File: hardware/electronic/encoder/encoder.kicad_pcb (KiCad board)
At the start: 2 copper layers, 26 x 29 mm, 10 parts, among them P1 CONN_01X04

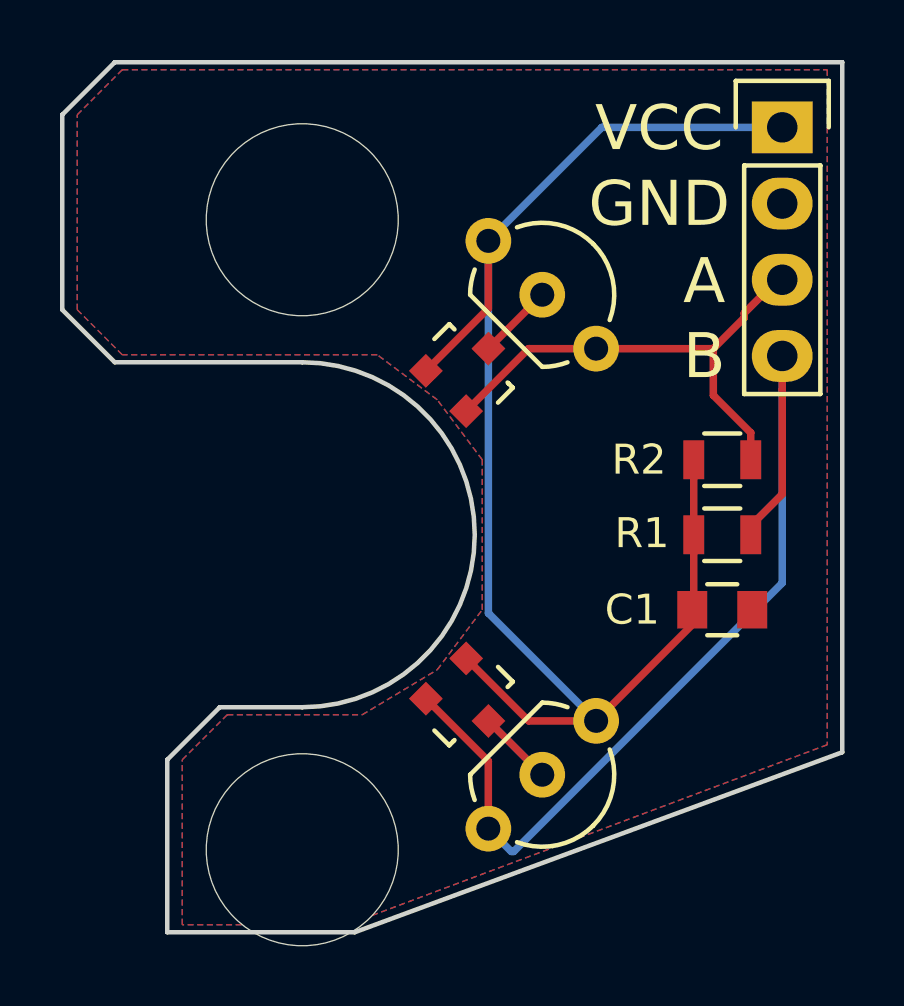
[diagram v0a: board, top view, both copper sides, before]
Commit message: HW: Start encoder rev-B
 - Remove smd footprints
 - Use bigger pads for passives
 - Fix missing connection
 - Improve hall effect footprint and silkscreen
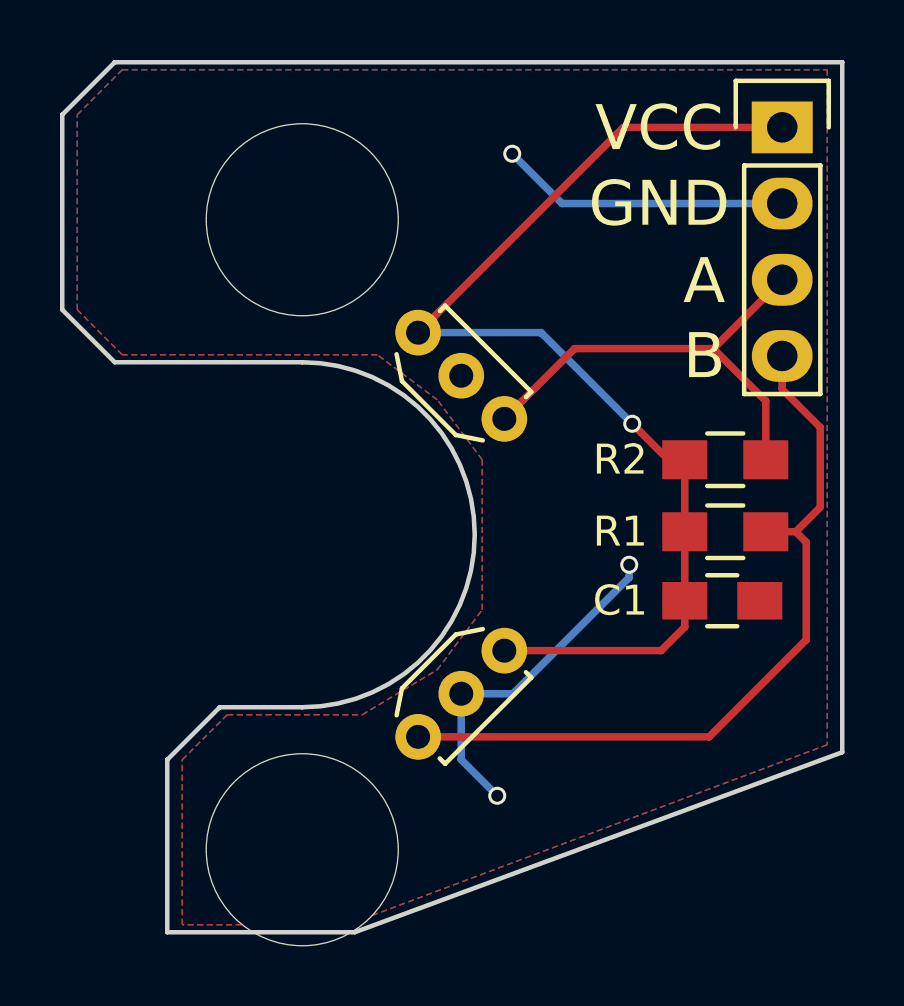
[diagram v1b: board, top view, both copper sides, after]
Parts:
- removed SOT-23-A1, SOT-23-B1: Digital_Latch_Hall_Effect_Sensor, TO_SOT_Packages_SMD:SOT-23
- C1: footprint Capacitors_SMD:C_0805 -> Capacitors_SMD:C_0805_HandSoldering
- R1, R2: footprint Resistors_SMD:R_0805 -> Resistors_SMD:R_0805_HandSoldering
- TO-92-A1, TO-92-B1: footprint TO_SOT_Packages_THT:TO-92_Inline_Wide -> OPAVES:DRV5013_Hall_Sensor_TO-92_Inline
- moved TO-92-A1 3.82 mm to (120.5, 69.4)
- moved TO-92-B1 3.82 mm to (124.1, 80.0)
- moved C1 0.30 mm to (131.0, 78.7)
- moved R1 0.14 mm to (131.1, 76.4)
- moved R2 0.10 mm to (131.1, 74.0)
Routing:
- net GND: track 5.07 -> 21.2 mm, vias 0 -> 3
- net VCC: track 49.3 -> 37.8 mm, vias 0 -> 1
- net B: track 33.1 -> 27.3 mm
- net A: track 16.7 -> 15.8 mm
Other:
- rule pad_to_mask_clearance: 0.2 -> 0.1
- board text added: "O'PAVES Motor encoder Rev-B"
- board text removed: "O'PAVES Motor encoder Rev-A"
